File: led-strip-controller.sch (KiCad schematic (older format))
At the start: 11 parts

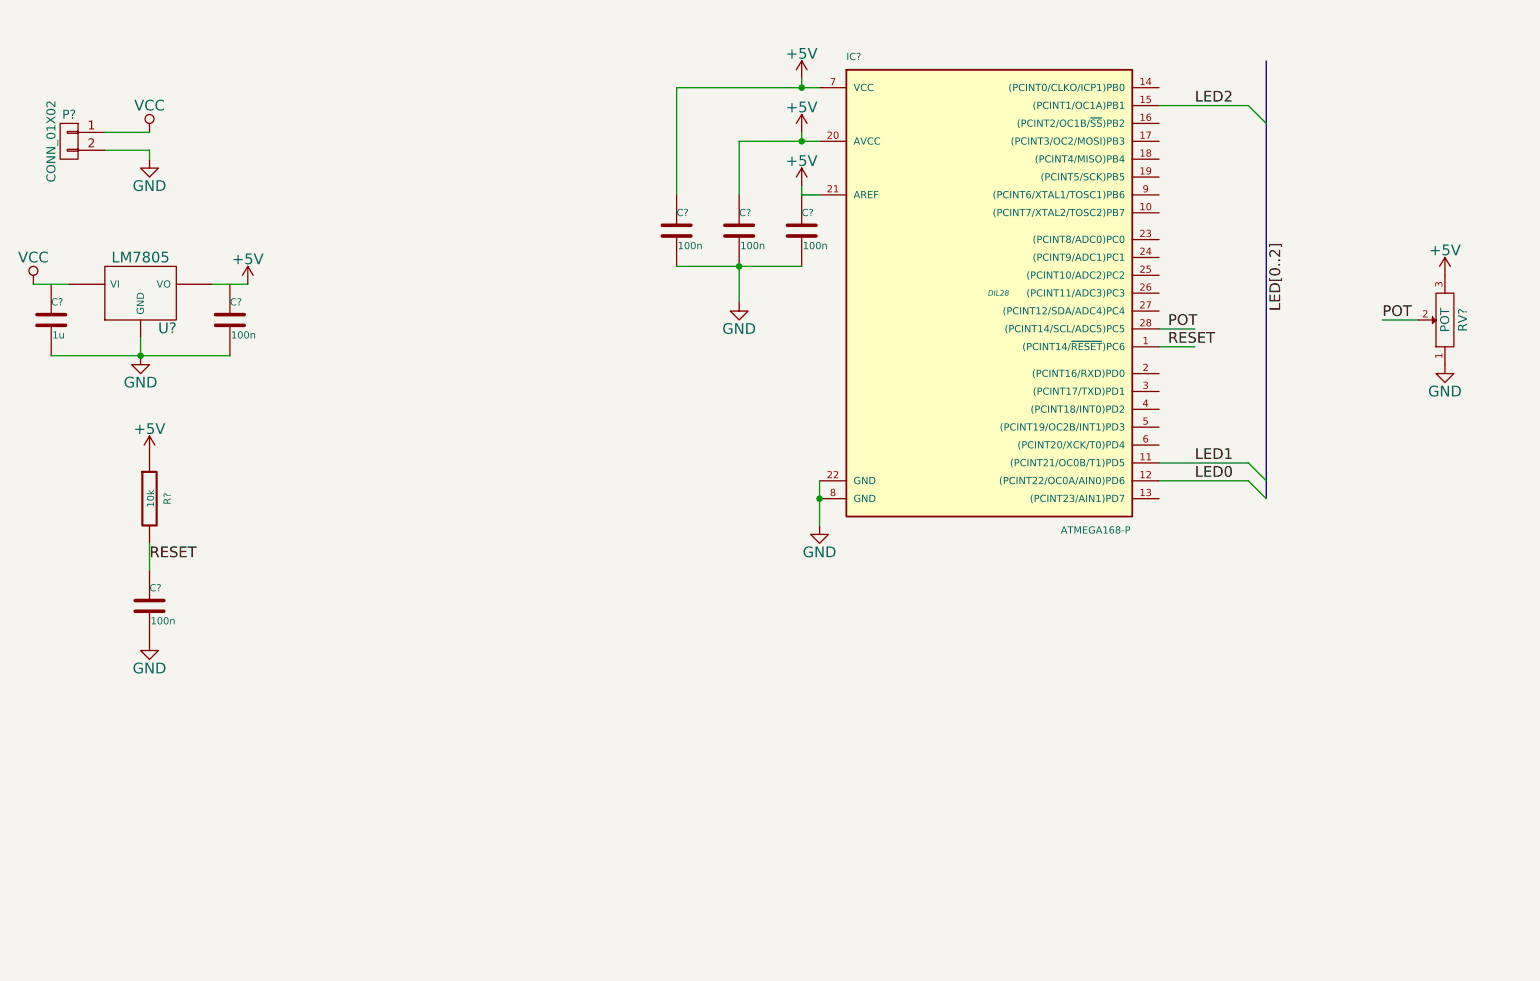
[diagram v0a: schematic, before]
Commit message: Added transistors which drive the LED strip
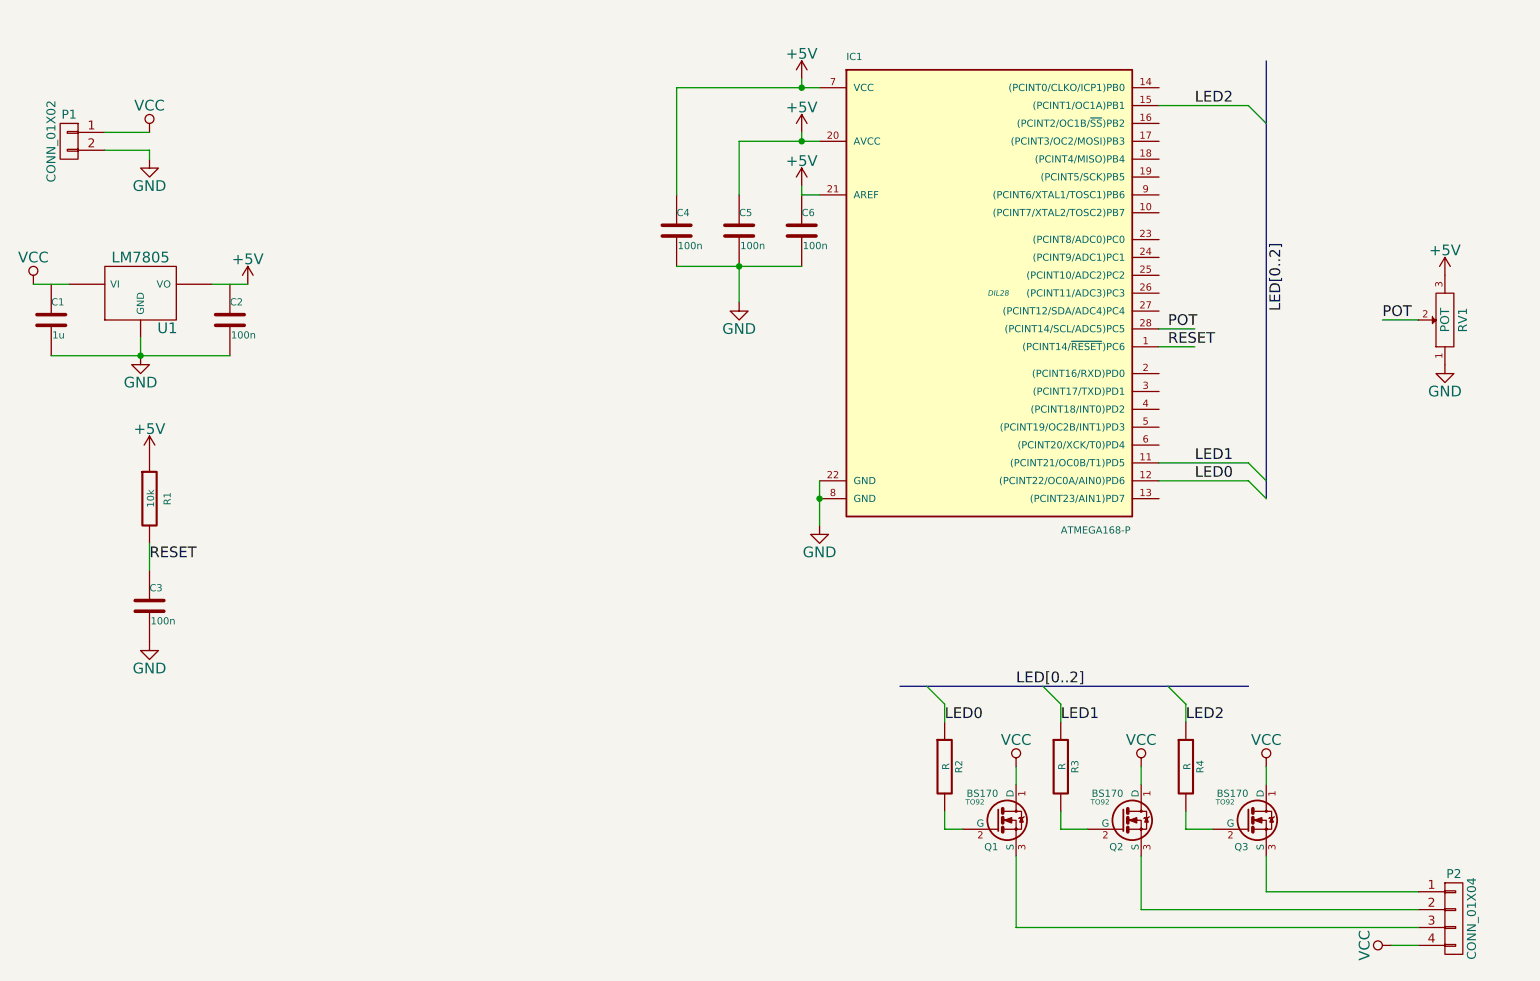
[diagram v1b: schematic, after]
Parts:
- added P2: CONN_01X04, symbol CONN_01X04
- added Q1, Q2, Q3: BS170, TO92, symbol BS170
- added R2, R3, R4: R, symbol R
- gave numbers to parts that had none: 11
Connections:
- wire segments 27 -> 46

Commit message: Changed LED connections matching the connections of the LED strip
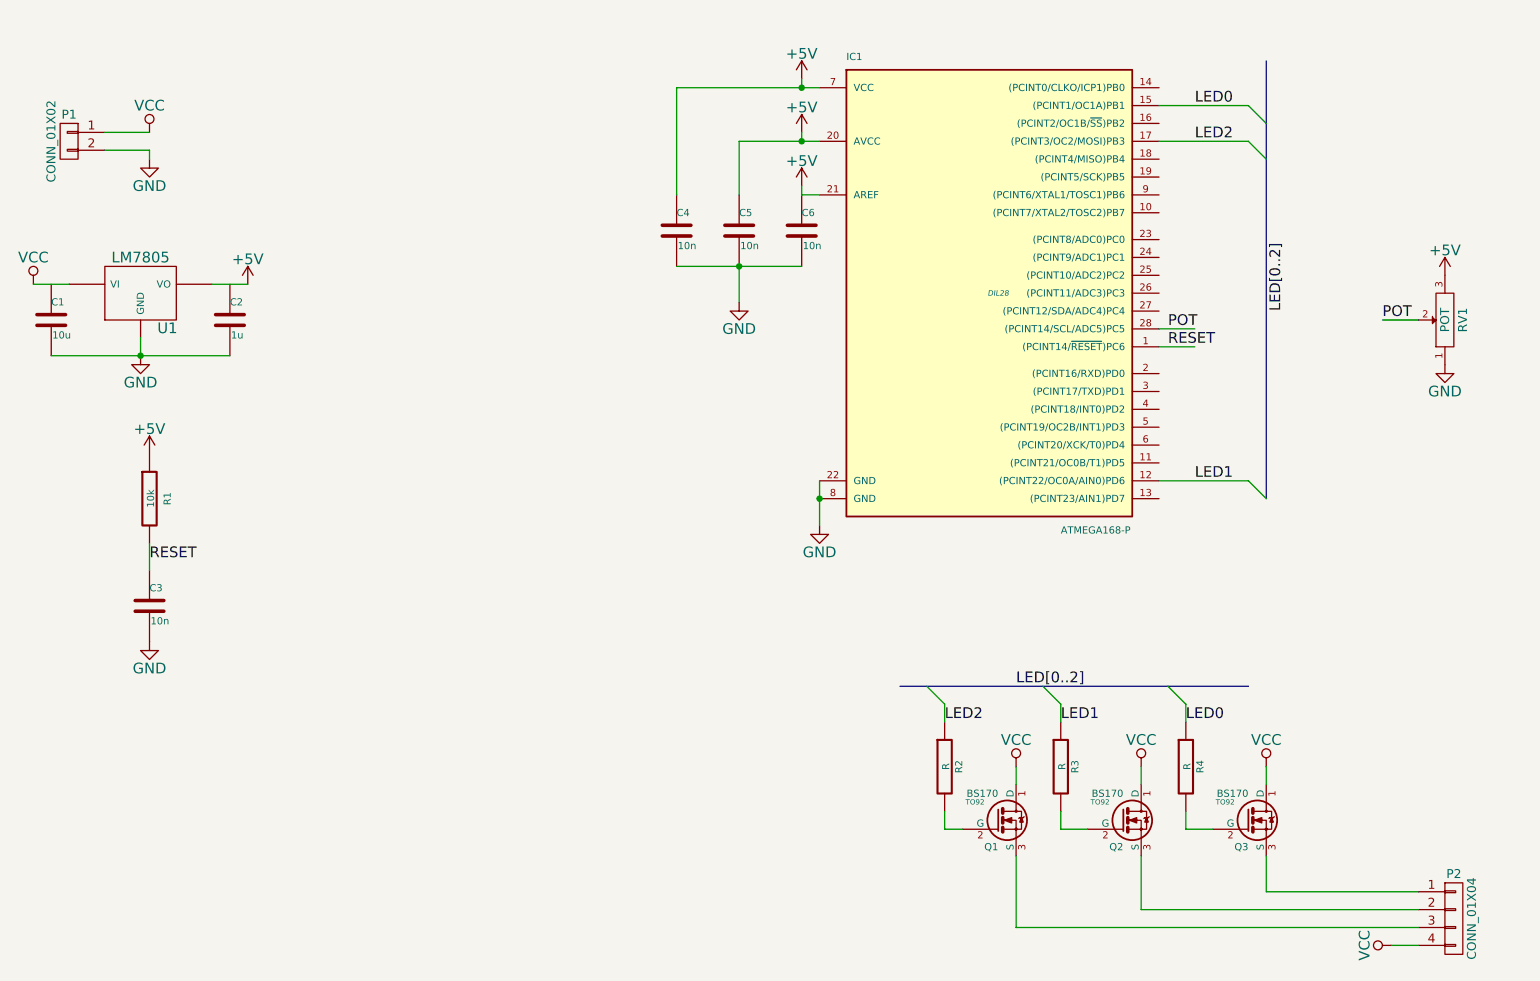
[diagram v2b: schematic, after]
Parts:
- C1: value 1u -> 10u
- C2: value 100n -> 1u
- C3, C4, C5, C6: value 100n -> 10n
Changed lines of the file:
@@
 P 5150 2150
 F 0 "C4" H 5150 2250 40  0000 L CNN
-F 1 "100n" H 5156 2065 40  0000 L CNN
+F 1 "10n" H 5156 2065 40  0000 L CNN
 F 2 "" H 5188 2000 30  0000 C CNN
 F 3 "" H 5150 2150 60  0000 C CNN
@@
 P 5500 2150
 F 0 "C5" H 5500 2250 40  0000 L CNN
-F 1 "100n" H 5506 2065 40  0000 L CNN
+F 1 "10n" H 5506 2065 40  0000 L CNN
 F 2 "" H 5538 2000 30  0000 C CNN
 F 3 "" H 5500 2150 60  0000 C CNN
@@
 P 5850 2150
 F 0 "C6" H 5850 2250 40  0000 L CNN
-F 1 "100n" H 5856 2065 40  0000 L CNN
+F 1 "10n" H 5856 2065 40  0000 L CNN
 F 2 "" H 5888 2000 30  0000 C CNN
 F 3 "" H 5850 2150 60  0000 C CNN
@@
 P 1650 2650
 F 0 "C1" H 1650 2750 40  0000 L CNN
-F 1 "1u" H 1656 2565 40  0000 L CNN
+F 1 "10u" H 1656 2565 40  0000 L CNN
 F 2 "" H 1688 2500 30  0000 C CNN
 F 3 "" H 1650 2650 60  0000 C CNN
@@
 P 2650 2650
 F 0 "C2" H 2650 2750 40  0000 L CNN
-F 1 "100n" H 2656 2565 40  0000 L CNN
+F 1 "1u" H 2656 2565 40  0000 L CNN
 F 2 "" H 2688 2500 30  0000 C CNN
 F 3 "" H 2650 2650 60  0000 C CNN
@@
 P 2200 4250
 F 0 "C3" H 2200 4350 40  0000 L CNN
-F 1 "100n" H 2206 4165 40  0000 L CNN
+F 1 "10n" H 2206 4165 40  0000 L CNN
 F 2 "" H 2238 4100 30  0000 C CNN
 F 3 "" H 2200 4250 60  0000 C CNN
@@
 	1    0    0    -1
 $EndComp
-Text Label 8050 3450 0    60   ~ 0
+Text Label 8050 3550 0    60   ~ 0
 LED1
-Text Label 8050 3550 0    60   ~ 0
-LED0
 Text Label 2200 4000 0    60   ~ 0
 RESET
@@
 RESET
 Entry Wire Line
-	8350 3450 8450 3550
-Entry Wire Line
 	8350 3550 8450 3650
 Entry Wire Line
 	8350 1450 8450 1550
 Text Label 8050 1450 0    60   ~ 0
-LED2
+LED0
 Text Label 8550 2600 1    60   ~ 0
 LED[0..2]
@@
 	7900 4700 8000 4800
 Text Label 6650 4900 0    60   ~ 0
-LED0
+LED2
 Text Label 7300 4900 0    60   ~ 0
 LED1
 Text Label 8000 4900 0    60   ~ 0
-LED2
+LED0
 $Comp
 L CONN_01X04 P2
@@
 Wire Wire Line
 	7850 3550 8350 3550
-Wire Wire Line
-	7850 3450 8350 3450
 Wire Wire Line
 	2200 3900 2200 4050
@@
 Wire Wire Line
 	9150 6150 9300 6150
+Wire Wire Line
+	7850 1650 8350 1650
+Entry Wire Line
+	8350 1650 8450 1750
+Text Label 8050 1650 0    60   ~ 0
+LED2
 $EndSCHEMATC

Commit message: Added barrel jack power connector
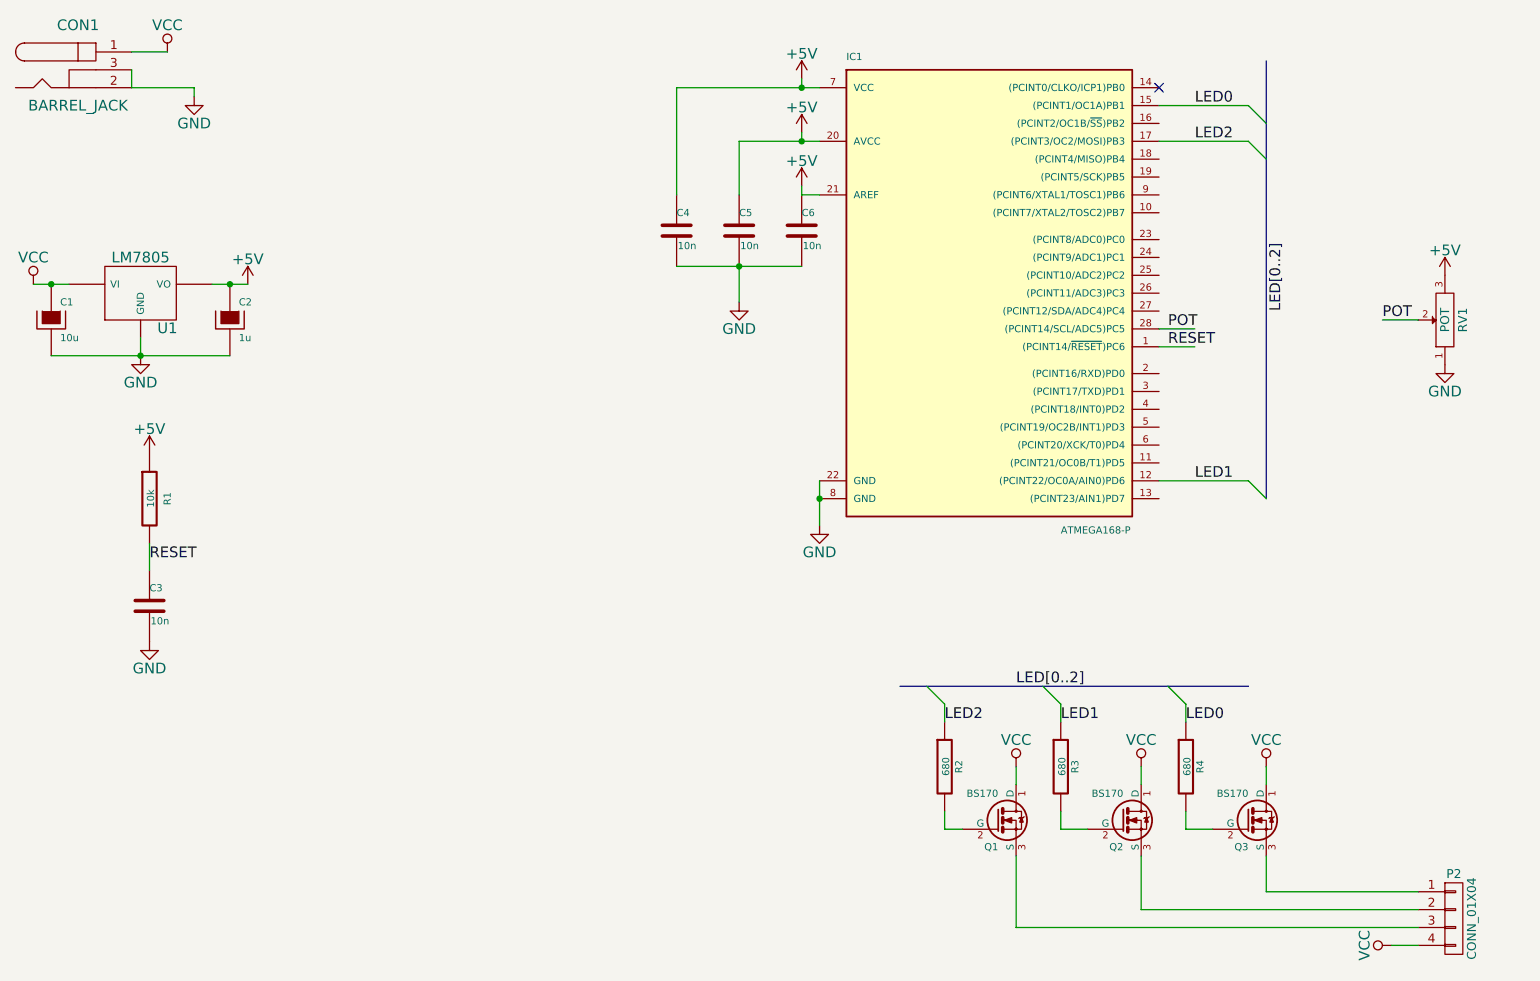
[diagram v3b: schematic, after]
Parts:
- removed C1: 10u, symbol C
- removed C2: 1u, symbol C
- removed P1: CONN_01X02, symbol CONN_01X02
- added C1: 10u, Capacitors_Elko_ThroughHole:Elko_vert_11.2x6.3mm_RM2.5, symbol CAPAPOL
- added C2: 1u, Capacitors_Elko_ThroughHole:Elko_vert_11.2x6.3mm_RM2.5, symbol CAPAPOL
- added CON1: BARREL_JACK, Connect:BARREL_JACK, symbol BARREL_JACK
- C3: footprint (none) -> Capacitors_ThroughHole:Capacitor6x11RM18
- C4, C5, C6: footprint (none) -> Capacitors_ThroughHole:Capacitor6MMDiscRM5
- IC1: footprint DIL28 -> Sockets_DIP:DIP-28__300_ELL
- P2: footprint (none) -> Pin_Headers:Pin_Header_Angled_1x04
- Q1, Q2, Q3: footprint TO92 -> Housings_TO-92:TO-92-FET-inline-narrow-oval-SGD
- R1: footprint (none) -> Resistors_ThroughHole:Resistor_Horizontal_RM15mm
- R2, R3, R4: value R -> 680; footprint (none) -> Resistors_ThroughHole:Resistor_Horizontal_RM15mm
- U1: footprint (none) -> Transistors_TO-220:TO-220_Neutral123_Horizontal
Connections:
- wire segments 46 -> 47
- no-connect marks 0 -> 1

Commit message: Use IRF640 as transistor to drive the LED strips
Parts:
- removed Q1, Q2, Q3: BS170, Housings_TO-92:TO-92-FET-inline-narrow-oval-SGD, symbol BS170
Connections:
- net labels added: B, G, R
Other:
- moved on the sheet: P2
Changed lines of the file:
@@
 POT
-$Comp
-L BS170 Q1
-U 1 1 54A17FBE
-P 6950 5450
-F 0 "Q1" H 6950 5301 40  0000 R CNN
-F 1 "BS170" H 6950 5600 40  0000 R CNN
-F 2 "Housings_TO-92:TO-92-FET-inline-narrow-oval-SGD" H 6820 5552 29  0001 C CNN
-F 3 "" H 6950 5450 60  0000 C CNN
-	1    6950 5450
-	1    0    0    -1
-$EndComp
-$Comp
-L BS170 Q2
-U 1 1 54A18895
-P 7650 5450
-F 0 "Q2" H 7650 5301 40  0000 R CNN
-F 1 "BS170" H 7650 5600 40  0000 R CNN
-F 2 "Housings_TO-92:TO-92-FET-inline-narrow-oval-SGD" H 7520 5552 29  0001 C CNN
-F 3 "" H 7650 5450 60  0000 C CNN
-	1    7650 5450
-	1    0    0    -1
-$EndComp
-$Comp
-L BS170 Q3
-U 1 1 54A188D4
-P 8350 5450
-F 0 "Q3" H 8350 5301 40  0000 R CNN
-F 1 "BS170" H 8350 5600 40  0000 R CNN
-F 2 "Housings_TO-92:TO-92-FET-inline-narrow-oval-SGD" H 8220 5552 29  0001 C CNN
-F 3 "" H 8350 5450 60  0000 C CNN
-	1    8350 5450
-	1    0    0    -1
-$EndComp
 $Comp
 L R R3
@@
 	1    0    0    -1
 $EndComp
-$Comp
-L VCC #PWR015
-U 1 1 54A1C1CF
-P 7050 5150
-F 0 "#PWR015" H 7050 5000 60  0001 C CNN
-F 1 "VCC" H 7050 5300 60  0000 C CNN
-F 2 "" H 7050 5150 60  0000 C CNN
-F 3 "" H 7050 5150 60  0000 C CNN
-	1    7050 5150
-	1    0    0    -1
-$EndComp
-$Comp
-L VCC #PWR016
-U 1 1 54A1C1F2
-P 7750 5150
-F 0 "#PWR016" H 7750 5000 60  0001 C CNN
-F 1 "VCC" H 7750 5300 60  0000 C CNN
-F 2 "" H 7750 5150 60  0000 C CNN
-F 3 "" H 7750 5150 60  0000 C CNN
-	1    7750 5150
-	1    0    0    -1
-$EndComp
-$Comp
-L VCC #PWR017
-U 1 1 54A1C20E
-P 8450 5150
-F 0 "#PWR017" H 8450 5000 60  0001 C CNN
-F 1 "VCC" H 8450 5300 60  0000 C CNN
-F 2 "" H 8450 5150 60  0000 C CNN
-F 3 "" H 8450 5150 60  0000 C CNN
-	1    8450 5150
-	1    0    0    -1
-$EndComp
 Text Label 7050 4700 0    60   ~ 0
 LED[0..2]
@@
 L CONN_01X04 P2
 U 1 1 54A20CE6
-P 9500 6000
-F 0 "P2" H 9500 6250 50  0000 C CNN
-F 1 "CONN_01X04" V 9600 6000 50  0000 C CNN
-F 2 "Pin_Headers:Pin_Header_Angled_1x04" H 9500 6000 60  0001 C CNN
-F 3 "" H 9500 6000 60  0000 C CNN
-	1    9500 6000
+P 9750 5200
+F 0 "P2" H 9750 5450 50  0000 C CNN
+F 1 "CONN_01X04" V 9850 5200 50  0000 C CNN
+F 2 "Pin_Headers:Pin_Header_Angled_1x04" H 9750 5200 60  0001 C CNN
+F 3 "" H 9750 5200 60  0000 C CNN
+	1    9750 5200
 	1    0    0    -1
 $EndComp
@@
 Wire Wire Line
 	6650 4800 6650 4900
-Wire Wire Line
-	8450 5650 8450 5850
-Wire Wire Line
-	8450 5850 9300 5850
-Wire Wire Line
-	7750 5650 7750 5950
-Wire Wire Line
-	7750 5950 9300 5950
-Wire Wire Line
-	7050 5650 7050 6050
-Wire Wire Line
-	7050 6050 9300 6050
 $Comp
 L VCC #PWR018
 U 1 1 54A21678
-P 9150 6150
-F 0 "#PWR018" H 9150 6000 60  0001 C CNN
-F 1 "VCC" H 9150 6300 60  0000 C CNN
-F 2 "" H 9150 6150 60  0000 C CNN
-F 3 "" H 9150 6150 60  0000 C CNN
-	1    9150 6150
+P 9400 5350
+F 0 "#PWR018" H 9400 5200 60  0001 C CNN
+F 1 "VCC" H 9400 5500 60  0000 C CNN
+F 2 "" H 9400 5350 60  0000 C CNN
+F 3 "" H 9400 5350 60  0000 C CNN
+	1    9400 5350
 	0    -1   -1   0
 $EndComp
 Wire Wire Line
-	9150 6150 9300 6150
+	9400 5350 9550 5350
 Wire Wire Line
 	7850 1650 8350 1650
@@
 Wire Wire Line
 	2100 1250 2100 1350
+Wire Wire Line
+	7050 5650 7050 5800
+Wire Wire Line
+	7750 5650 7750 5800
+Wire Wire Line
+	8450 5650 8450 5800
+$Comp
+L GND #PWR?
+U 1 1 54AEB316
+P 7050 5800
+F 0 "#PWR?" H 7050 5550 60  0001 C CNN
+F 1 "GND" H 7050 5650 60  0000 C CNN
+F 2 "" H 7050 5800 60  0000 C CNN
+F 3 "" H 7050 5800 60  0000 C CNN
+	1    7050 5800
+	1    0    0    -1
+$EndComp
+$Comp
+L GND #PWR?
+U 1 1 54AEB38E
+P 7750 5800
+F 0 "#PWR?" H 7750 5550 60  0001 C CNN
+F 1 "GND" H 7750 5650 60  0000 C CNN
+F 2 "" H 7750 5800 60  0000 C CNN
+F 3 "" H 7750 5800 60  0000 C CNN
+	1    7750 5800
+	1    0    0    -1
+$EndComp
+$Comp
+L GND #PWR?
+U 1 1 54AEB3AB
+P 8450 5800
+F 0 "#PWR?" H 8450 5550 60  0001 C CNN
+F 1 "GND" H 8450 5650 60  0000 C CNN
+F 2 "" H 8450 5800 60  0000 C CNN
+F 3 "" H 8450 5800 60  0000 C CNN
+	1    8450 5800
+	1    0    0    -1
+$EndComp
+Wire Wire Line
+	9550 5050 9350 5050
+Wire Wire Line
+	9550 5150 9350 5150
+Wire Wire Line
+	9550 5250 9350 5250
+Text Label 9400 5050 0    60   ~ 0
+G
+Text Label 9400 5150 0    60   ~ 0
+R
+Text Label 9400 5250 0    60   ~ 0
+B
+Text Label 8450 5150 0    60   ~ 0
+G
+Text Label 7750 5150 0    60   ~ 0
+R
+Text Label 7050 5150 0    60   ~ 0
+B
 $EndSCHEMATC
